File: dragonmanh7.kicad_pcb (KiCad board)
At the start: 4 copper layers, 135.6 x 54.6 mm, 145 parts, among them J1 USB_B, J10 Conn_02x12_Odd_Even, J11 Conn_02x05_Odd_Even, J12 VBAT+, J13 Conn_02x05_Odd_Even, J14 VBATG, J15 Conn_02x02_Odd_Even, J16 Conn_02x02_Odd_Even, J18 Conn_02x05_Odd_Even, J2 73725-0110BLF, J3 RJ45_Amphenol_RJMG1BD3B8K1ANR, J4 105162-0001, J5 Screw_Terminal_01x06, J6 Conn_02x12_Odd_Even, J7 USB_B, J8 Screw_Terminal_01x02, J9 Conn_02x12_Odd_Even, SW1 RESET, SW2 PC13, U1 STM32H743VITx, U10 USBLC6-2SC6, U12 TCAN332, U13 ISL83483, U14 MIC2005A, U2 LAN8742A-CZ-TR, U3 AZ1117CD-3.3TRG1, U5 S25FL127SABMFI101, U6 AP63205, U7 USBLC6-2SC6, U8 STM32F042F6Px, U9 USBLC6-2SC6, Y1 8MHz, Y2 32.768KHz, Y3 25MHz

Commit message: Point of save
Signed-off-by: Martin Ribelotta <martinribelotta@gmail.com>
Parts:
- moved R9 1.48 mm to (142.8, 79.2)
- moved D7 0.64 mm to (141.0, 79.2)
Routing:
- net /PC2: track 45.6 -> 50.2 mm, vias 0 -> 1
- net GND: track 210.8 -> 212.3 mm
- net /~RESET: track 138.5 -> 139.9 mm, vias 3 -> 2
- net Net-(D7-Pad1): track 3.08 -> 1.86 mm
- net +3V3: track 172.1 -> 173.1 mm
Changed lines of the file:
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@@
     (thickness 1.6)
     (drawings 54)
-    (tracks 3371)
+    (tracks 3375)
     (zones 0)
     (modules 145)
@@
   )
   (module Resistor_SMD:R_0603_1608Metric (layer F.Cu)
-    (at 144.1196 79.883 270)
+    (at 142.7988 79.2226 270)
     (descr "Resistor SMD 0603 (1608 Metric), square (rectangular) end terminal, IPC_7351 nominal, (Body size source: http://www.tortai-tech.com/upload/download/2011102023233369053.pdf), generated with kicad-footprint-generator")
     (tags resistor)
@@
   )
   (module LED_SMD:LED_0805_2012Metric_Castellated (layer F.Cu)
-    (at 141.0462 79.883 90)
+    (at 141.0208 79.248 90)
     (descr "LED SMD 0805 (2012 Metric), castellated end terminal, IPC_7351 nominal, (Body size source: https://docs.google.com/spreadsheets/d/1BsfQQcO9C6DZCsRaXUlFlo91Tg2WpOkGARC1WS5S8t0/edit?usp=sharing), generated with kicad-footprint-generator")
     (tags "LED castellated")
@@
   (segment (start 146.2785 72.1613) (end 146.2532 72.136) (width 0.25) (layer F.Cu) (net 1))
   (segment (start 146.2785 73.3552) (end 146.2785 72.1613) (width 0.25) (layer F.Cu) (net 1))
-  (via (at 139.9032 78.9178) (size 0.8) (drill 0.4) (layers F.Cu B.Cu) (net 1))
-  (segment (start 141.0462 78.9205) (end 139.9059 78.9205) (width 0.25) (layer F.Cu) (net 1))
-  (segment (start 139.9059 78.9205) (end 139.9032 78.9178) (width 0.25) (layer F.Cu) (net 1))
   (segment (start 99.4895 61.5129) (end 99.4582 61.5442) (width 0.9) (layer F.Cu) (net 1))
   (segment (start 99.4895 56.9468) (end 99.4895 61.5129) (width 0.9) (layer F.Cu) (net 1))
@@
   (segment (start 145.7111 29.0616) (end 145.7111 29.9726) (width 0.6) (layer F.Cu) (net 1))
   (segment (start 145.542 28.8925) (end 145.7111 29.0616) (width 0.6) (layer F.Cu) (net 1))
+  (via (at 139.4968 76.7842) (size 0.8) (drill 0.4) (layers F.Cu B.Cu) (net 1))
+  (segment (start 141.0208 78.2855) (end 139.5195 76.7842) (width 0.25) (layer F.Cu) (net 1))
+  (segment (start 139.5195 76.7842) (end 139.4968 76.7842) (width 0.25) (layer F.Cu) (net 1))
   (via (at 143.51 68.5165) (size 0.8) (drill 0.4) (layers F.Cu B.Cu) (net 2))
   (via (at 143.51 66.9925) (size 0.8) (drill 0.4) (layers F.Cu B.Cu) (net 2))
@@
   (segment (start 177.263458 48.020602) (end 177.263458 48.28794) (width 0.25) (layer F.Cu) (net 2))
   (via (at 177.263458 48.28794) (size 0.8) (drill 0.4) (layers F.Cu B.Cu) (net 2))
-  (segment (start 146.2786 80.137) (end 147.6968 80.137) (width 0.25) (layer F.Cu) (net 2))
-  (segment (start 144.1196 78.9455) (end 145.0871 78.9455) (width 0.25) (layer F.Cu) (net 2))
-  (segment (start 145.0871 78.9455) (end 146.2786 80.137) (width 0.25) (layer F.Cu) (net 2))
   (segment (start 107.3785 78.74) (end 109.22 78.74) (width 0.25) (layer F.Cu) (net 2))
   (segment (start 106.7689 78.1304) (end 107.3785 78.74) (width 0.25) (layer F.Cu) (net 2))
@@
   (via (at 170.8785 43.8034) (size 0.8) (drill 0.4) (layers F.Cu B.Cu) (net 2))
   (segment (start 170.8785 44.8055) (end 170.8785 43.8034) (width 0.25) (layer F.Cu) (net 2))
+  (segment (start 142.7988 78.4351) (end 143.6625 78.4351) (width 0.25) (layer F.Cu) (net 2))
+  (segment (start 145.3644 80.137) (end 147.6968 80.137) (width 0.25) (layer F.Cu) (net 2))
+  (segment (start 143.6625 78.4351) (end 145.3644 80.137) (width 0.25) (layer F.Cu) (net 2))
   (segment (start 135.545281 55.410141) (end 135.545281 57.339539) (width 0.25) (layer F.Cu) (net 3))
   (segment (start 135.545281 57.339539) (end 134.84606 58.03876) (width 0.25) (layer F.Cu) (net 3))
@@
   (segment (start 116.74094 50.05832) (end 118.351588 48.447672) (width 0.25) (layer F.Cu) (net 31))
   (segment (start 114.71172 53.06568) (end 115.59286 53.06568) (width 0.25) (layer F.Cu) (net 31))
-  (via (at 115.6335 77.406498) (size 0.8) (drill 0.4) (layers F.Cu B.Cu) (net 31))
-  (segment (start 152.1968 80.137) (end 150.996799 81.337001) (width 0.25) (layer F.Cu) (net 31))
-  (segment (start 146.080075 81.337001) (end 144.601084 79.85801) (width 0.25) (layer F.Cu) (net 31))
-  (segment (start 150.996799 81.337001) (end 146.080075 81.337001) (width 0.25) (layer F.Cu) (net 31))
-  (segment (start 144.601084 79.85801) (end 143.638116 79.85801) (width 0.25) (layer F.Cu) (net 31))
-  (segment (start 143.638116 79.85801) (end 141.186604 77.406498) (width 0.25) (layer F.Cu) (net 31))
-  (segment (start 141.186604 77.406498) (end 115.6335 77.406498) (width 0.25) (layer F.Cu) (net 31))
-  (segment (start 109.22 76.2) (end 110.426498 77.406498) (width 0.25) (layer B.Cu) (net 31))
-  (segment (start 110.426498 77.406498) (end 115.6335 77.406498) (width 0.25) (layer B.Cu) (net 31))
   (segment (start 163.4617 44.577) (end 161.81621 42.93151) (width 0.25) (layer B.Cu) (net 31))
   (segment (start 139.75799 42.93151) (end 135.42264 47.26686) (width 0.25) (layer B.Cu) (net 31))
@@
   (segment (start 169.164 49.874) (end 169.164 47.994298) (width 0.25) (layer B.Cu) (net 31))
   (segment (start 164.719 45.847) (end 166.8145 45.847) (width 0.25) (layer B.Cu) (net 31))
+  (segment (start 110.426498 77.406498) (end 109.22 76.2) (width 0.25) (layer F.Cu) (net 31))
+  (segment (start 110.426498 79.743298) (end 110.426498 77.406498) (width 0.25) (layer F.Cu) (net 31))
+  (segment (start 111.4298 80.7466) (end 110.426498 79.743298) (width 0.25) (layer F.Cu) (net 31))
+  (segment (start 138.557 80.7466) (end 111.4298 80.7466) (width 0.25) (layer F.Cu) (net 31))
+  (segment (start 139.147401 81.337001) (end 138.557 80.7466) (width 0.25) (layer F.Cu) (net 31))
+  (segment (start 150.996799 81.337001) (end 139.147401 81.337001) (width 0.25) (layer F.Cu) (net 31))
+  (segment (start 152.1968 80.137) (end 150.996799 81.337001) (width 0.25) (layer F.Cu) (net 31))
   (segment (start 130.72364 61.9339) (end 130.72364 60.9473) (width 0.25) (layer F.Cu) (net 32))
   (segment (start 131.24865 62.45891) (end 130.72364 61.9339) (width 0.25) (layer F.Cu) (net 32))
@@
   (segment (start 118.613869 49.510141) (end 118.563879 49.56013) (width 0.25) (layer F.Cu) (net 73))
   (segment (start 117.795902 50.328107) (end 117.795902 55.742545) (width 0.25) (layer F.Cu) (net 73))
-  (segment (start 113.124999 77.375001) (end 114.3 76.2) (width 0.25) (layer F.Cu) (net 73))
-  (segment (start 113.124999 80.194401) (end 113.124999 77.375001) (width 0.25) (layer F.Cu) (net 73))
-  (segment (start 104.902 81.036) (end 112.2834 81.036) (width 0.25) (layer F.Cu) (net 73))
-  (segment (start 112.2834 81.036) (end 113.124999 80.194401) (width 0.25) (layer F.Cu) (net 73))
+  (segment (start 103.92699 80.06099) (end 103.92699 75.21921) (width 0.25) (layer F.Cu) (net 73))
+  (segment (start 104.902 81.036) (end 103.92699 80.06099) (width 0.25) (layer F.Cu) (net 73))
+  (segment (start 103.92699 75.21921) (end 104.4194 74.7268) (width 0.25) (layer F.Cu) (net 73))
+  (segment (start 106.6546 74.7268) (end 107.1372 75.2094) (width 0.25) (layer F.Cu) (net 73))
+  (segment (start 104.4194 74.7268) (end 106.6546 74.7268) (width 0.25) (layer F.Cu) (net 73))
+  (via (at 107.1372 75.2094) (size 0.8) (drill 0.4) (layers F.Cu B.Cu) (net 73))
+  (segment (start 112.909401 74.809401) (end 114.3 76.2) (width 0.25) (layer B.Cu) (net 73))
+  (segment (start 107.537199 74.809401) (end 112.909401 74.809401) (width 0.25) (layer B.Cu) (net 73))
+  (segment (start 107.1372 75.2094) (end 107.537199 74.809401) (width 0.25) (layer B.Cu) (net 73))
   (segment (start 116.82222 76.18222) (end 116.84 76.2) (width 0.25) (layer F.Cu) (net 74))
   (segment (start 116.82222 74.75474) (end 116.82222 76.18222) (width 0.25) (layer F.Cu) (net 74))
@@
   (segment (start 128.045281 39.610141) (end 128.045281 36.683462) (width 0.25) (layer F.Cu) (net 110))
   (segment (start 104.902 79.111) (end 104.902 77.328) (width 0.25) (layer F.Cu) (net 111))
-  (segment (start 141.0712 80.8205) (end 141.0462 80.8455) (width 0.25) (layer F.Cu) (net 112))
-  (segment (start 144.1196 80.8205) (end 141.0712 80.8205) (width 0.25) (layer F.Cu) (net 112))
+  (segment (start 141.0208 80.2105) (end 141.8109 80.2105) (width 0.25) (layer F.Cu) (net 112))
+  (segment (start 142.0113 80.0101) (end 142.7988 80.0101) (width 0.25) (layer F.Cu) (net 112))
+  (segment (start 141.8109 80.2105) (end 142.0113 80.0101) (width 0.25) (layer F.Cu) (net 112))
   (segment (start 143.498 65.8172) (end 143.498 65.05999) (width 0.25) (layer F.Cu) (net 113))
   (segment (start 145.73109 62.8269) (end 146.47916 62.8269) (width 0.25) (layer F.Cu) (net 113))

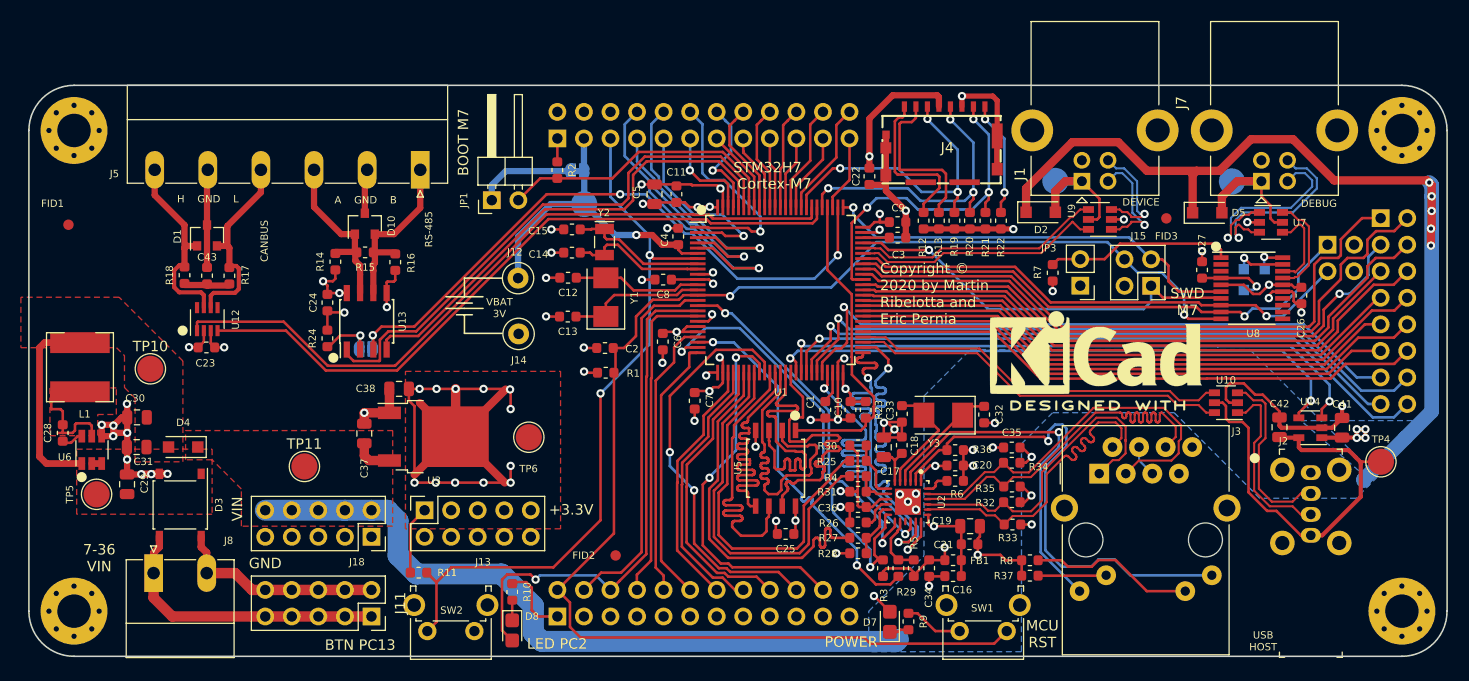
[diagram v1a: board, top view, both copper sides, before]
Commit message: Move rigth side expansion to center
Signed-off-by: Martin Ribelotta <martinribelotta@gmail.com>
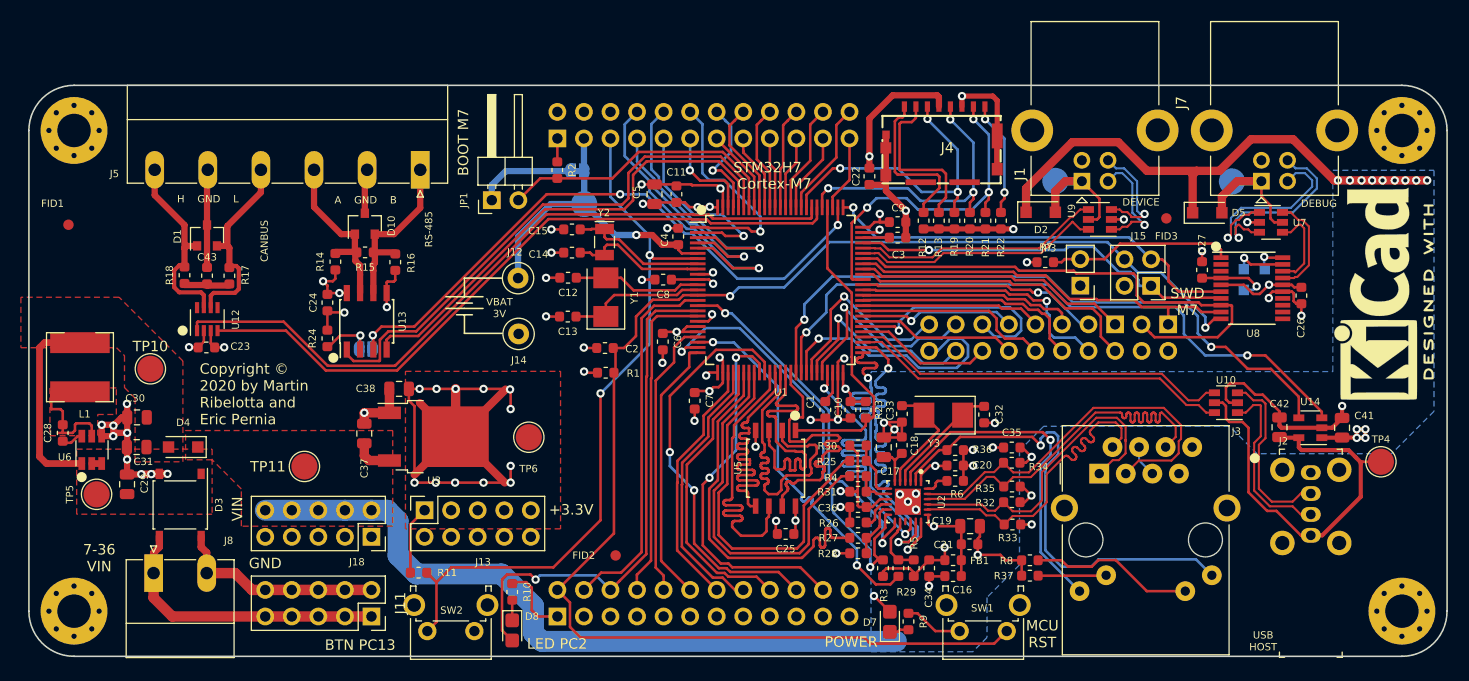
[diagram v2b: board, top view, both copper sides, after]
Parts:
- moved J6 27.4 mm to (162.6, 50.8), turned to 90 degrees
- moved LOGO1 27.3 mm to (187.5, 47.9), turned to 90 degrees
- moved J16 17.0 mm to (167.6, 50.8), turned to 90 degrees
- moved R7 1.24 mm to (155.9, 44.9), turned to 0 degrees
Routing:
- net /PE15: track 63.8 -> 19.5 mm
- net /PD8: track 55.0 -> 13.1 mm
- net /PE14: track 60.9 -> 19.0 mm
- net /PB10: track 61.8 -> 20.4 mm
- net /PD10: track 55.7 -> 15.1 mm
- net /PE13: track 63.6 -> 25.2 mm
- net +5V: track 168.2 -> 130.1 mm, vias 9 -> 13
- net /PD11: track 53.0 -> 15.0 mm, vias 0 -> 1
- net /PD12: track 56.4 -> 18.7 mm
- net /PD13: track 53.7 -> 17.3 mm
- net /PD14: track 57.8 -> 22.2 mm
- net /PD15: track 55.1 -> 20.8 mm
- net /PC7: track 57.1 -> 23.1 mm
- net /PA8: track 60.2 -> 26.3 mm
- net /PC6: track 59.1 -> 25.6 mm, vias 0 -> 1
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
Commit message: Saved point
Signed-off-by: Martin Ribelotta <martinribelotta@gmail.com>
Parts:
- moved FID3 15.6 mm to (183.0, 41.2)
- moved C22 5.92 mm to (139.4, 30.7)
- moved R37 1.78 mm to (152.6, 74.8)
- moved R8 1.78 mm to (152.6, 73.3)
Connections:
- net Net-(C12-Pad1) renamed /8MHz+
- net Net-(C13-Pad1) renamed /8MHz-
- net Net-(C14-Pad1) renamed /32K+
- net Net-(C15-Pad1) renamed /32K-
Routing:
- net +3V3: track 173.1 -> 167.3 mm
- net /SDMMC_CLK: track 28.0 -> 33.2 mm
- net /SDMMC_CMD: track 29.1 -> 33.1 mm
- net Net-(J3-PadL2): track 15.8 -> 17.6 mm
- net Net-(J3-PadL3): track 6.52 -> 8.29 mm
- net /PE15: track 19.5 -> 17.8 mm
- net /USB_SER_D+: track 8.32 -> 9.81 mm
- net GND: track 212.6 -> 211.4 mm
- net /~RESET: track 140.1 -> 139.1 mm
- net /SWCLK: track 40.8 -> 39.9 mm
- net /8MHz-: track 13.3 -> 12.6 mm
- net /PB10: track 20.4 -> 19.8 mm
- net /PD15: track 20.8 -> 20.2 mm
- net /SDMMC_D0: track 32.6 -> 33.2 mm
- net /PC13: track 69.2 -> 69.8 mm
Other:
- board text added: "+"
- board text added: "-"

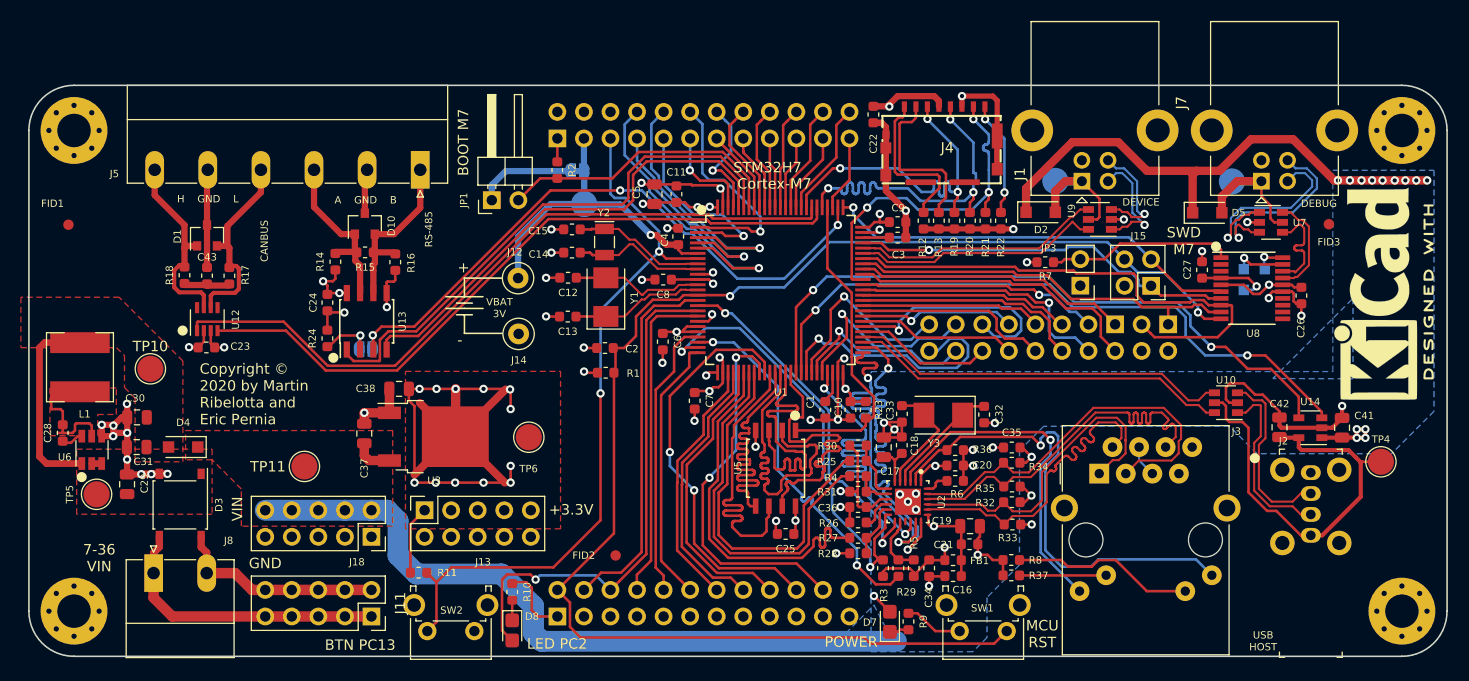
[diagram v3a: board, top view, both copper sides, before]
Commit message: Add ESD filters to uSD connector, improve routing
Signed-off-by: Martin Ribelotta <martinribelotta@gmail.com>
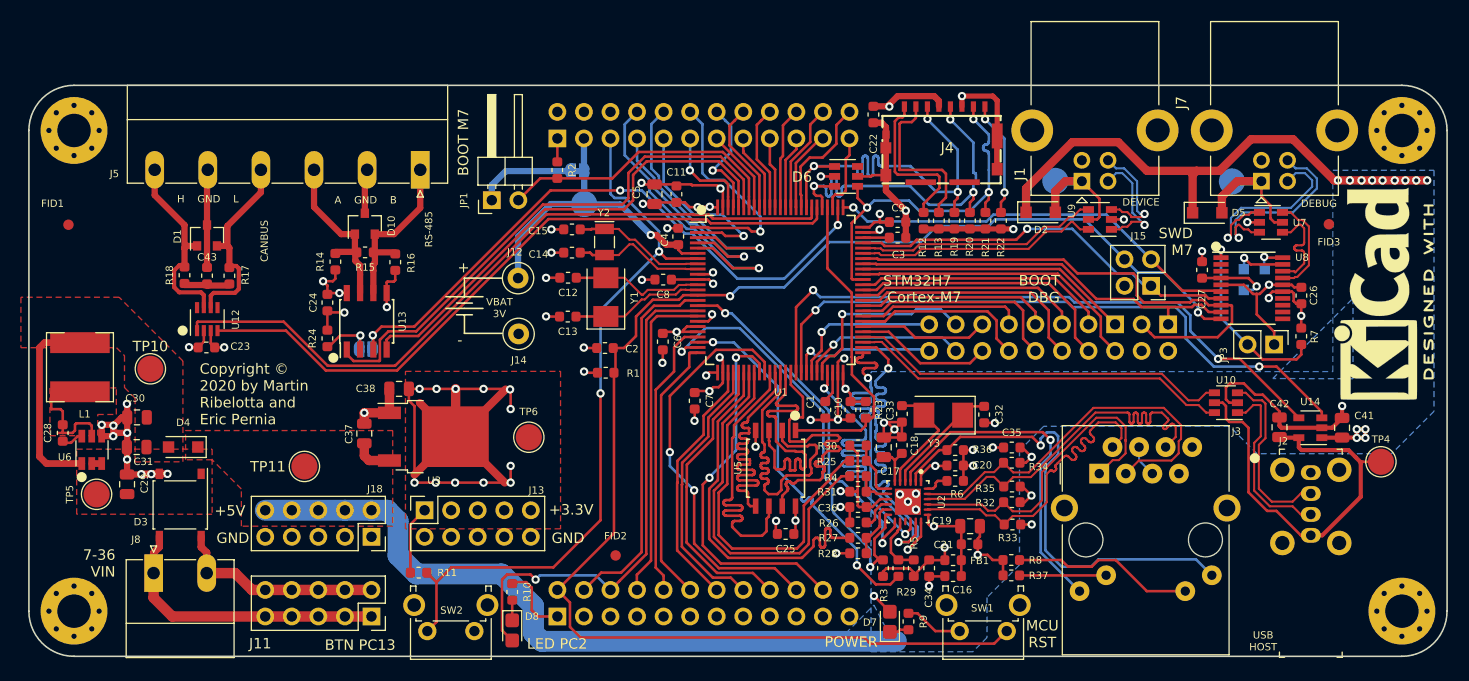
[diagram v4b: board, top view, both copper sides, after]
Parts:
- added D6: ESDA6V1BC6, Package_TO_SOT_SMD:SOT-23-6, F.Cu at (136.8, 36.7)
- moved R7 25.5 mm to (180.4, 51.9), turned to 270 degrees
- moved JP3 19.4 mm to (177.8, 52.7), turned to 270 degrees
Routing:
- net /PE13: track 25.2 -> 14.1 mm
- net /PD9: track 22.7 -> 12.4 mm, vias 1 -> 0
- net /SDMMC_CMD: track 33.1 -> 39.3 mm
- net +3V3: track 167.3 -> 172.8 mm
- net /SDMMC_CLK: track 33.2 -> 37.7 mm
- net /PD10: track 15.1 -> 19.5 mm
- net GND: track 211.4 -> 215.7 mm
- net /PE14: track 19.0 -> 14.9 mm
- net /SDMMC_D0: track 33.2 -> 35.5 mm
- net /PE11: track 62.9 -> 61.0 mm
- net /PE15: track 17.8 -> 15.8 mm
- net /~RESET: track 139.1 -> 140.9 mm
- net /PD12: track 18.7 -> 20.4 mm
- net /PB10: track 19.8 -> 18.3 mm
- net /PD13: track 17.3 -> 18.6 mm
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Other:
- board text added: "+5V"
- board text added: "BOOT DBG"
- board text removed: "VIN"
